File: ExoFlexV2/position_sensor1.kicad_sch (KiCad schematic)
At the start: 27 parts

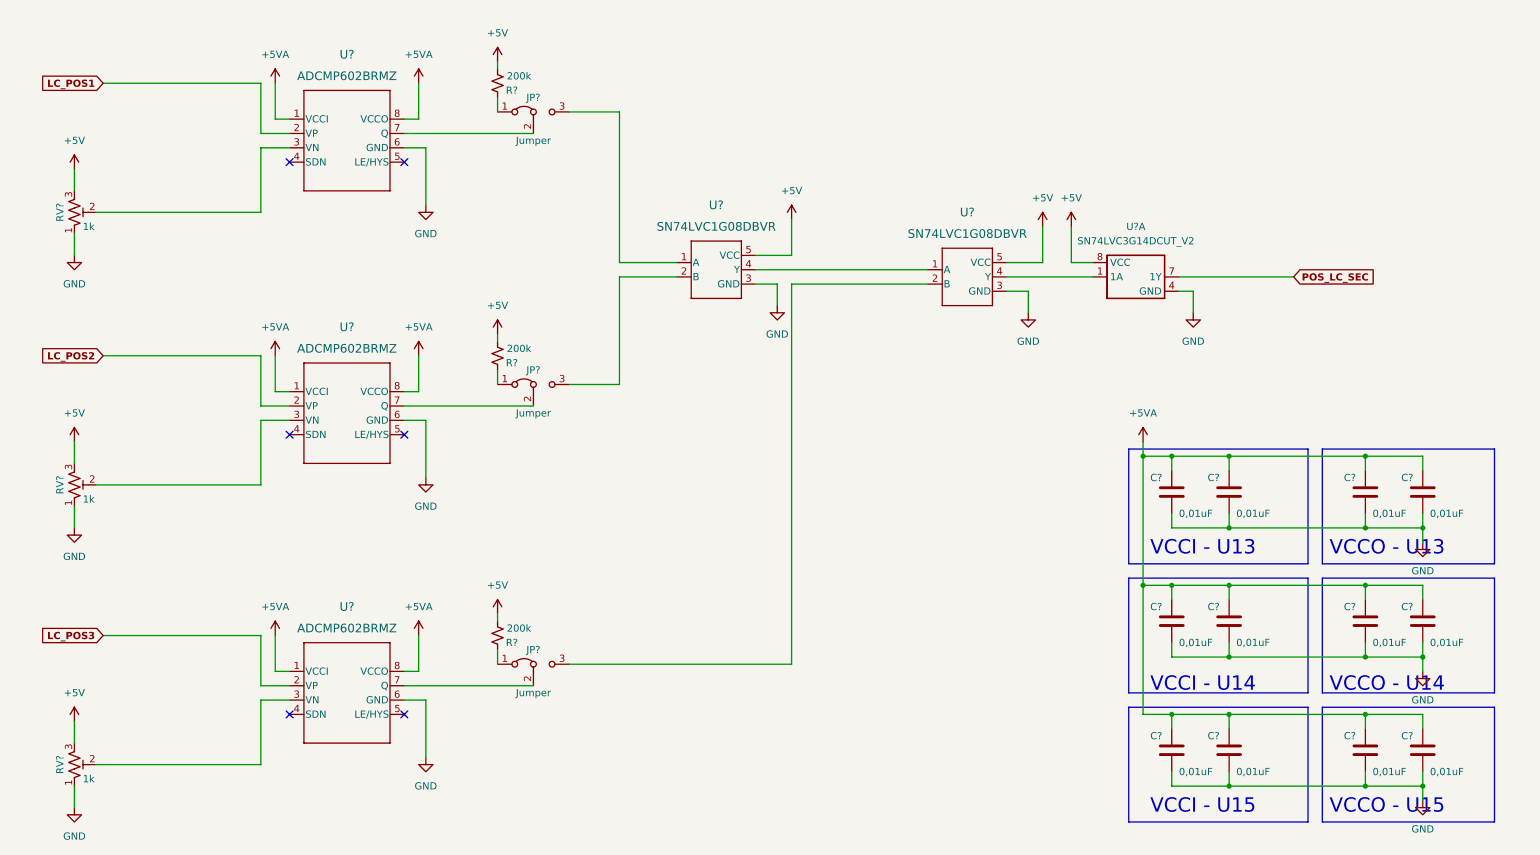
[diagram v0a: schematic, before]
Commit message: Mise à jour signaux STM
- Condo de découplage
- Signaux supplémentaire pour le STM
- Page GND sera pour Multiplexeur
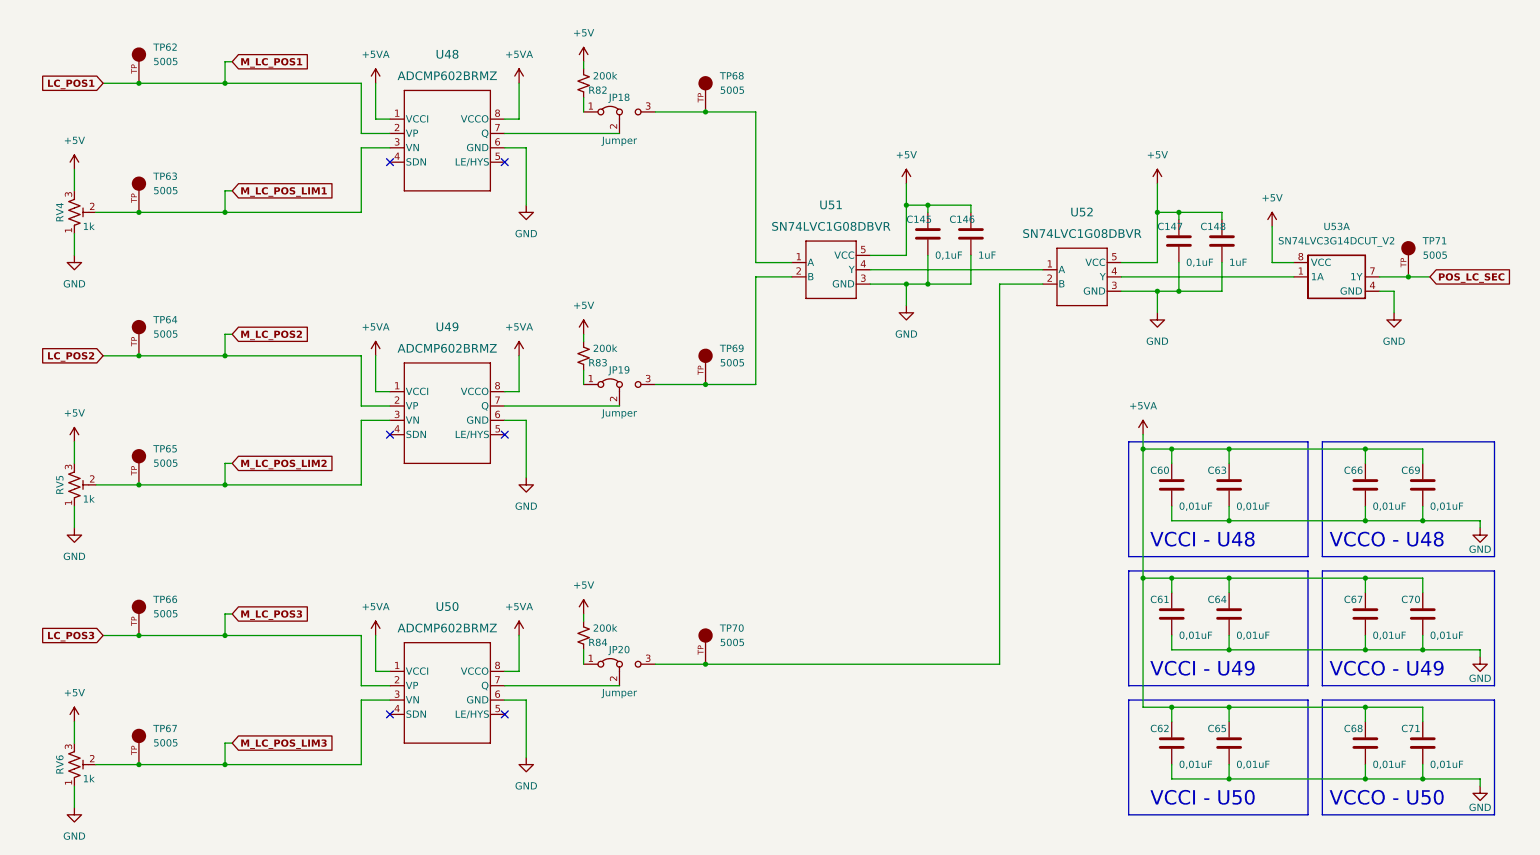
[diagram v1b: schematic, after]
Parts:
- added C145, C147: 0,1uF, Capacitor_SMD:C_0603_1608Metric, symbol Device:C
- added C146, C148: 1uF, Capacitor_SMD:C_0603_1608Metric, symbol Device:C
- added TP62, TP63, TP64, TP65, TP66, TP67, TP68, TP69, TP70, TP71: 5005, FootPrint:KEYSTONE_5005, symbol SymLib:5005
- gave numbers to parts that had none: 27
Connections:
- net +5V: now also C145.1, C146.1, C147.1, C148.1
- net GND: now also C145.2, C146.2, C147.2, C148.2
- net LC_POS1: now also TP62.TP
- net LC_POS2: now also TP64.TP
- net LC_POS3: now also TP66.TP
- net POS_LC_SEC: now also TP71.TP
- net at JP19.3 (B), U51.2 (B): now also TP69.TP
- net at JP20.3 (B), U52.2 (B): now also TP70.TP
- net M_LC_POS_LIM3: now reaches RV6.2, U50.3 (VN)
- net M_LC_POS_LIM3: now also TP67.TP
- net M_LC_POS_LIM1: now reaches RV4.2, U48.3 (VN)
- net M_LC_POS_LIM1: now also TP63.TP
- net M_LC_POS_LIM2: now reaches RV5.2, U49.3 (VN)
- net M_LC_POS_LIM2: now also TP65.TP
- net at JP18.3 (B), U51.1 (A): now also TP68.TP
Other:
- note added: "VCCI - U48"
- note added: "VCCI - U49"
- note added: "VCCI - U50"
- note added: "VCCO - U48"
- note added: "VCCO - U49"
- note added: "VCCO - U50"
- note removed: "VCCI - U13"
- note removed: "VCCI - U14"
- note removed: "VCCI - U15"
- note removed: "VCCO - U13"
- note removed: "VCCO - U14"
- note removed: "VCCO - U15"
- moved on the sheet: C60, C61, C62, C63, C64, C65, C66, C67, C68, C69, C70, C71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

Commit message: Finalisation 1
- Ajout de pages pour la gestion des signaux négatif
- Modification des pages de torque et amplitude
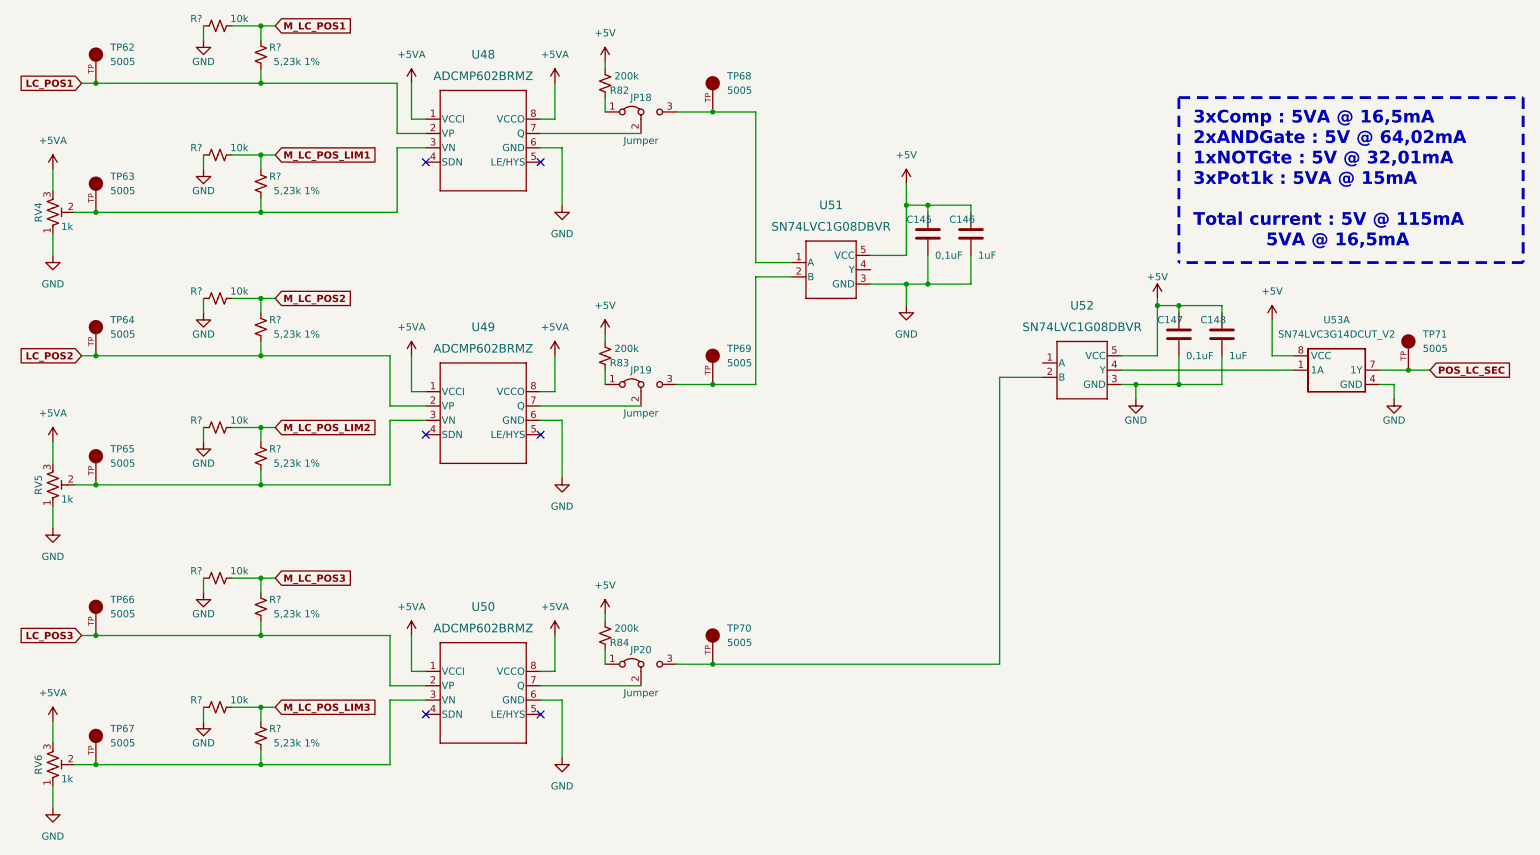
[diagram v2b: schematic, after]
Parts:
- removed C60, C61, C62, C63, C64, C65, C66, C67, C68, C69, C70, C71: 0,01uF, Capacitor_SMD:C_0603_1608Metric, symbol Device:C
- added R? (x6): 5,23k 1%, Resistor_SMD:R_0805_2012Metric, symbol Device:R_Small_US
- added R? (x6): 10k, Resistor_SMD:R_0805_2012Metric, symbol Device:R_Small_US
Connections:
- net +5V: no longer RV4.3, RV5.3, RV6.3
- net +5VA: now also RV4.3, RV5.3, RV6.3
- net GND: now also R?.1, R?.1, R?.1, R?.1, R?.1, R?.1
- net LC_POS1: now also R?.2
- net LC_POS2: now also R?.2
- net LC_POS3: now also R?.2
- net M_LC_POS_LIM1: now also R?.1, R?.2; no longer RV4.2, TP63.TP, U48.3 (VN)
- net M_LC_POS_LIM2: now also R?.1, R?.2; no longer RV5.2, TP65.TP, U49.3 (VN)
- net M_LC_POS_LIM3: now also R?.1, R?.2; no longer RV6.2, TP67.TP, U50.3 (VN)
- net at U52.1 (A): no longer U51.4 (Y)
- new net: R?.2, RV6.2, TP67.TP, U50.3 (VN)
- new net: R?.2, RV4.2, TP63.TP, U48.3 (VN)
- new net: R?.2, RV5.2, TP65.TP, U49.3 (VN)
- new net M_LC_POS1: R?.1, R?.2
- new net M_LC_POS2: R?.1, R?.2
- new net M_LC_POS3: R?.1, R?.2
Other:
- note added: "3xComp : 5VA @ 16,5mA 2xANDGate : 5V @ 64,02mA 1xNOTGte : 5V @ 32,01mA 3xPot1k : 5VA @ 15mA Total current : 5V @ 115mA 5VA @ 16,5mA"
- note removed: "VCCI - U48"
- note removed: "VCCI - U49"
- note removed: "VCCI - U50"
- note removed: "VCCO - U48"
- note removed: "VCCO - U49"
- note removed: "VCCO - U50"
- moved on the sheet: C147, C148, JP18, JP19, JP20, R82, R83, R84, RV4, RV5, RV6, TP62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
